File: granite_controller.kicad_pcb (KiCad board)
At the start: 4 copper layers, 230 x 40 mm, 204 parts, among them J1 HR911105A, J10 DRY_IN, J11 MB01_FP, J12 MB02_FP, J13 MB03_FP, J14 MB04_FP, J15 MB05_FP, J16 MB06_FP, J17 MB07_FP, J18 MB08_FP, J2 USB4105-xx-A, J3 19V_IN, J4 1WIRE, J5 1WIRE, J6 1WIRE, J7 1WIRE, J8 EXPANSION, J9 I2C_SENSOR, K1 TLP176AM, K10 TLP176AM, K11 TLP176AM, K12 TLP176AM, K13 TLP176AM, K14 TLP176AM, K15 TLP176AM, K16 TLP176AM, K2 TLP176AM, K3 TLP176AM, K4 TLP176AM, K5 TLP176AM, K6 TLP176AM, K7 TLP176AM, K8 TLP176AM, K9 TLP176AM, U1 ESP32-C6-WROOM-1-N8, U14 MCP23017-E/SO, U15 MCP23017-E/SO, U16 TLP290-4, U17 TLP290-4, U18 TPD4E05U06DQA, U2 TLV62569DBV, U3 W5500, U4 USBLC6-2SC6, U5 TMP1075D, U6 TPD4E05U06DQA, U7 TPD4E05U06DQA, U8 LMR51430YDDCR, Y2 25MHz 12pF YXC

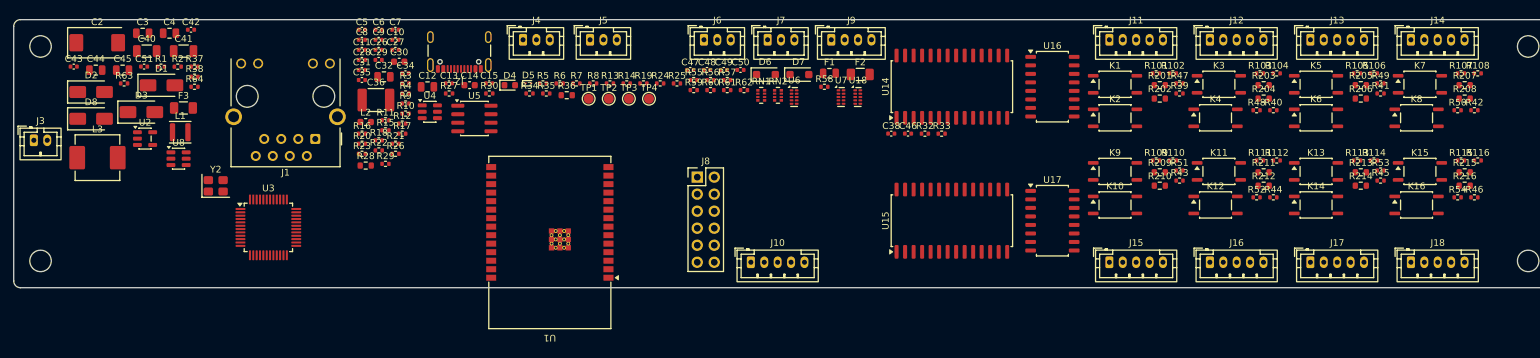
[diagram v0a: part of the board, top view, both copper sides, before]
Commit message: Tidy silkscreen after placement
tools/silk.py moves values to F.Fab, hides silk refs on small passives and
places the remaining refs clear of pads, silk outlines and courtyards,
connectors first. Silk DRC is clean apart from U1's intentional antenna
overhang. place.py keeps a label lane under J6/J7/J9.
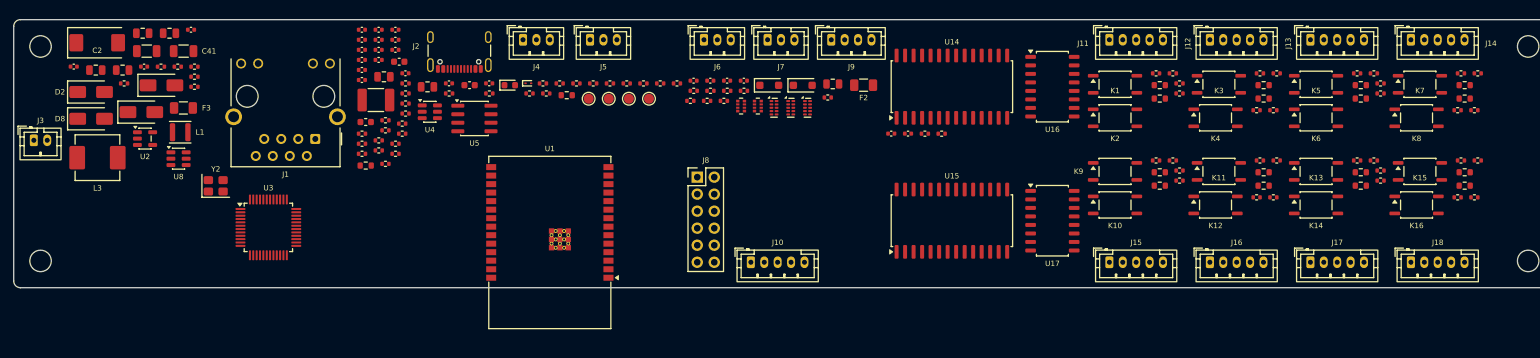
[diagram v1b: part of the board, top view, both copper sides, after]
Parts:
- moved R59 20.0 mm to (121.5, 11.6)
- moved R58 12.0 mm to (109.0, 10.6)
- moved U18 7.67 mm to (118.5, 13.1)
- moved U7 7.67 mm to (116.0, 13.1)
- moved R60 3.40 mm to (101.0, 12.1)
- moved R61 3.40 mm to (103.5, 12.1)
- moved R62 3.40 mm to (106.0, 12.1)
- moved RN1 3.40 mm to (108.5, 12.9)
- moved RN2 3.40 mm to (111.0, 12.9)
- moved U6 3.40 mm to (113.5, 13.1)
- moved C47 1.68 mm to (101.5, 9.11)
- moved C48 1.68 mm to (104.0, 9.11)
- moved C49 1.68 mm to (106.5, 9.11)
- moved C50 1.68 mm to (109.0, 9.11)
- moved D6 1.68 mm to (112.7, 9.79)
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
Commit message: 250 x 50 board, Ethernet placement, KRT routing, outer GND pours
- place.py: 250 x 50 mm with a 0.8 mm packing gap; Ethernet chain placed
  in line (W5500 rotated so its PHY pins face the RJ45, 33R row,
  termination/coupling row, crystal under XI/XO); label lanes under the
  top-edge connectors.
- setrules.py: signal vias 0.5/0.2, power/GND 0.6/0.3.
- krt_route.sh: KiCadRoutingTools chain on a copy outside the repo
  (planes, Ethernet and USB pairs, then the rest on F.Cu/B.Cu only).
- gndpour.py: GND pours on F.Cu/B.Cu plus 118 stitching vias.
- Board: user's hand placement, routed and poured. DRC: 0 parity, 21
  unconnected, 3 undersized vias at the W5500 crossovers, 11 dangling
  vias; see docs/handoff.md.
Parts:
- moved C27 71.1 mm to (74.4, 73.4), turned to 90 degrees
- moved C26 70.1 mm to (67.6, 73.4), turned to 90 degrees
- moved U5 69.7 mm to (129.5, 48.9)
- moved R27 65.3 mm to (123.0, 41.0)
- moved U6 63.6 mm to (170.0, 42.2)
- moved Y2 63.5 mm to (71.0, 73.4)
- moved RN2 63.1 mm to (167.0, 42.0)
- moved C11 62.9 mm to (58.0, 67.1)
- moved R30 62.7 mm to (126.0, 41.0)
- moved RN1 62.7 mm to (164.0, 42.0)
- moved R3 62.2 mm to (62.5, 71.6)
- moved R35 62.2 mm to (134.5, 40.1)
- moved C10 62.1 mm to (58.0, 65.1)
- moved J18 61.6 mm to (256.5, 74.8)
- moved C7 61.2 mm to (61.0, 62.6)
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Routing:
- net GND: track 0.00 -> 228.7 mm, vias 0 -> 191
- net +5V: track 0.00 -> 164.8 mm, vias 0 -> 9
- net I2C_INT_SDA: track 0.00 -> 153.2 mm, vias 0 -> 8
- net I2C_INT_SCL: track 0.00 -> 152.4 mm, vias 0 -> 12
- net EXP_INT: track 0.00 -> 136.1 mm, vias 0 -> 10
- net /Relay channels/NODE_ON8: track 0.00 -> 131.6 mm, vias 0 -> 4
- net VIN_SENSE: track 0.00 -> 129.4 mm, vias 0 -> 5
- net EXP_nRESET_INT: track 0.00 -> 123.7 mm, vias 0 -> 8
- net /Relay channels/RST_DRV4: track 0.00 -> 112.1 mm, vias 0 -> 8
- net /Relay channels/PWR_DRV4: track 0.00 -> 111.5 mm, vias 0 -> 10
- net /Relay channels/NODE_ON4: track 0.00 -> 111.2 mm, vias 0 -> 9
- net /Relay channels/PWR_DRV8: track 0.00 -> 104.7 mm, vias 0 -> 8
- net +3V3: track 0.00 -> 103.5 mm, vias 0 -> 36
- net /Relay channels/NODE_ON2: track 0.00 -> 102.9 mm, vias 0 -> 12
- net /Relay channels/NODE_ON3: track 0.00 -> 99.3 mm, vias 0 -> 10
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- added copper zone on In2.Cu, net +3V3
- added copper zone on B.Cu, net GND
- added copper zone on F.Cu, net GND
- added copper zone on In1.Cu, net GND
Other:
- board size 230 x 40 mm -> 250 x 50 mm

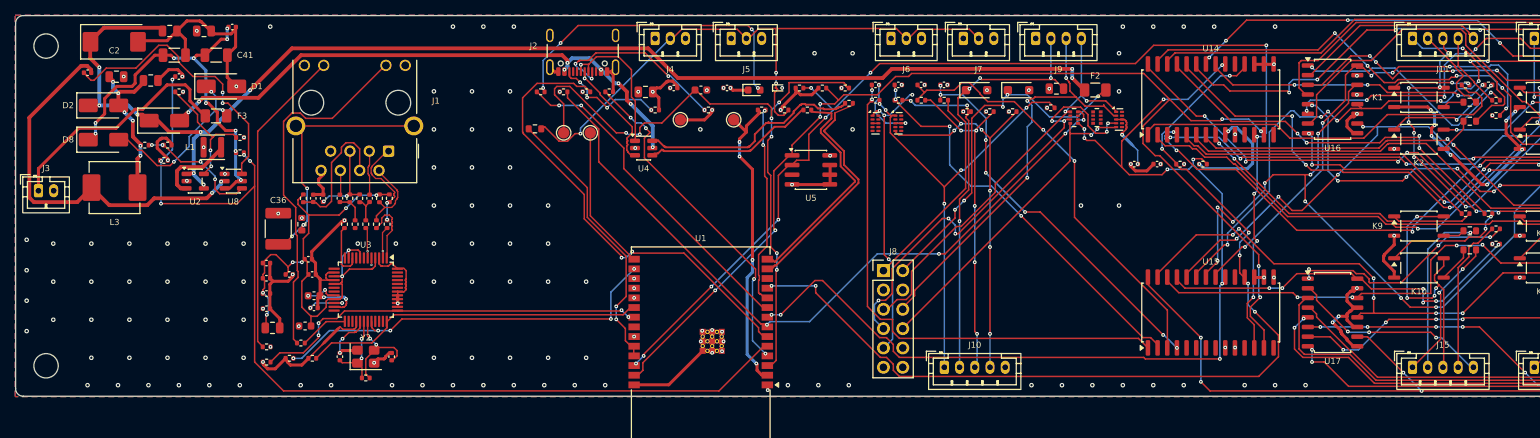
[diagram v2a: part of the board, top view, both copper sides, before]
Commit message: Targeted KRT reroute of the open nets; handoff update
Ripped and re-routed the 16 open signal nets with everything else kept,
then a GND pass without rip-up. Closed ETH_RXN, USB_CONN_D+ and HDR_IO5:
21 -> 18 unconnected, violations unchanged (27). The rest is blocked by
neighbouring copper and the RN1/RN2/U7/U18 pad field around J8.

docs/handoff.md: current board state, next steps (spread J8 area, re-run
the targeted pass, hand-route critical nets) and the pod/duck
architecture under discussion.
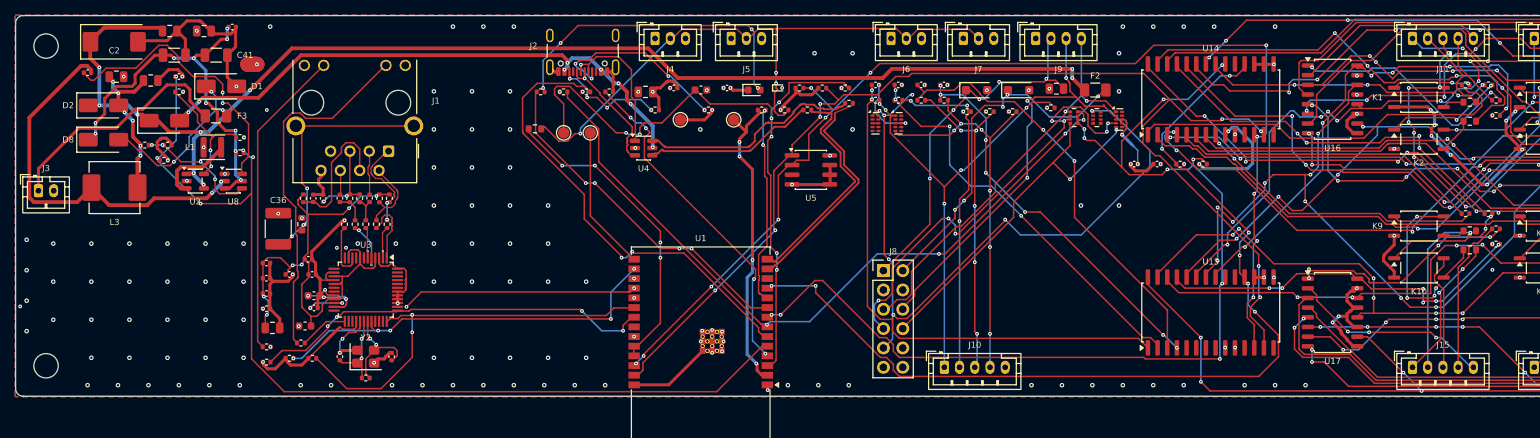
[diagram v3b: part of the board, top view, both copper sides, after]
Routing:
- net /Expansion header/HDR_IO5: track 38.4 -> 94.1 mm, vias 4 -> 7
- net ETH_MOSI: track 0.00 -> 30.9 mm, vias 1 -> 2
- net GND: track 228.7 -> 244.8 mm, vias 191 -> 197
- net ETH_INT: track 44.4 -> 54.7 mm, vias 0 -> 2
- net /Expansion header/HDR_INT: track 42.7 -> 48.7 mm
- net /Ethernet/ETH_RXN: track 0.05 -> 5.71 mm, vias 1 -> 2
- net /MCU/OW_MCU: track 36.4 -> 40.3 mm, vias 2 -> 4
- net /Ethernet/+3V3A: track 70.5 -> 67.8 mm, vias 8 -> 6
- net VIN_SENSE: track 129.4 -> 127.3 mm
- net /MCU/LED_HB: track 43.1 -> 45.1 mm, vias 2 -> 4
- net /MCU/USB_CONN_D+: track 15.9 -> 17.5 mm
- net ETH_RST: track 51.2 -> 52.4 mm
- net /Expansion header/HDR_3V3: track 47.8 -> 47.7 mm, vias 3 -> 5

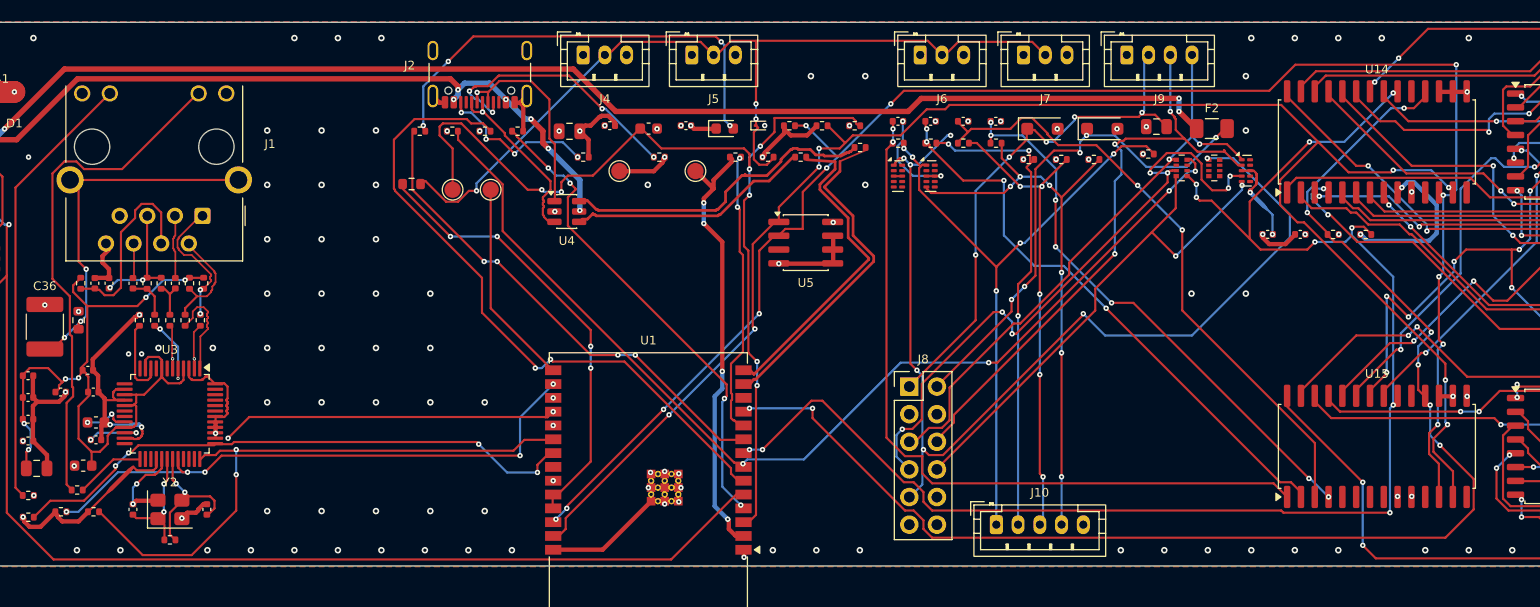
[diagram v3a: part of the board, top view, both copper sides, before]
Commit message: Spread the J8 part field and rerun the targeted KRT pass
Moved RN1/RN2 between U1 and J8 (rot 180, MCU side facing U1), U7 next to
J8 pins 9-11 and U18 above J10. Strapped the TPD4E05 centre GND pads to a
plane via, cleared all copper of the 22 affected nets (KRT's own rip left
stubs) and rerouted them, then a GND pass. DRC: 18 -> 7 unconnected,
27 -> 23 violations, 0 parity, no shorts or dangling tracks.

tools/krt_reroute.sh captures the targeted pass for next time.
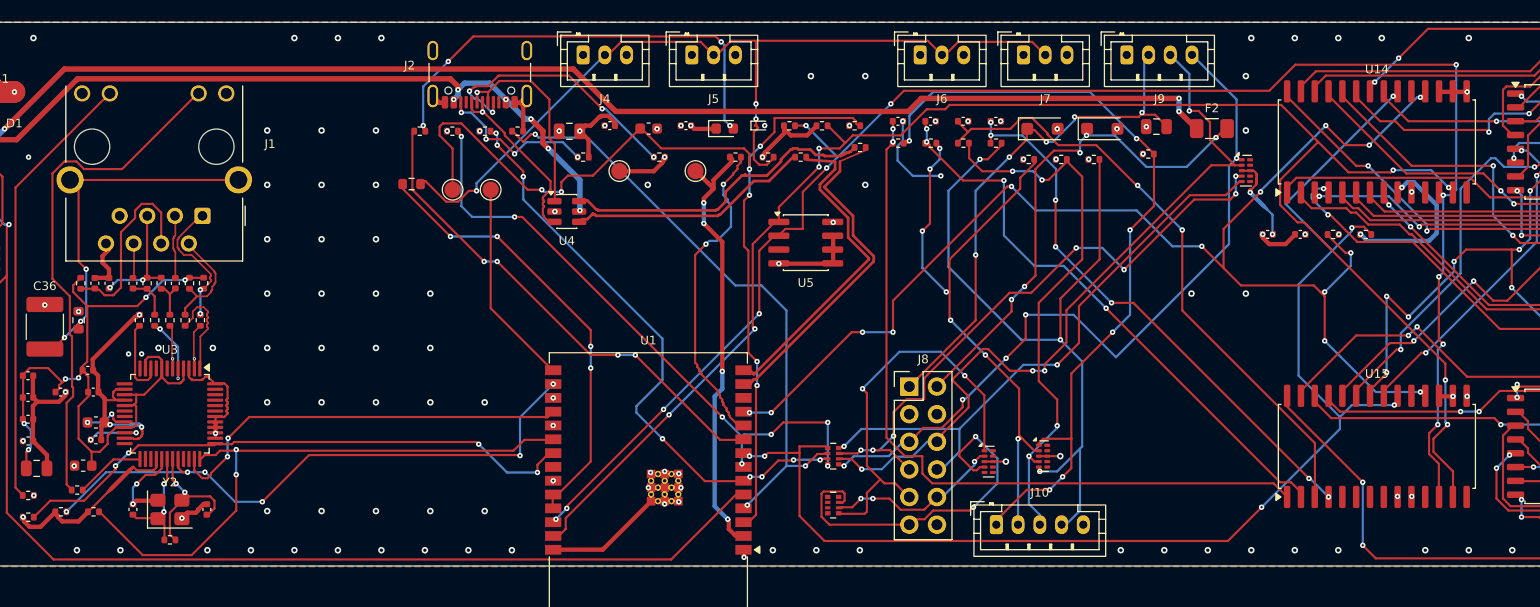
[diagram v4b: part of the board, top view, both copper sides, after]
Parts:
- moved RN2 46.8 mm to (132.0, 73.0), turned to 180 degrees
- moved RN1 41.6 mm to (132.0, 68.5), turned to 180 degrees
- moved U18 27.8 mm to (151.3, 68.5)
- moved U7 27.5 mm to (146.3, 69.0)
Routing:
- net /Expansion header/HDR_IO5: track 94.1 -> 37.9 mm, vias 7 -> 2
- net I2C_EXT_SCL: track 96.1 -> 56.3 mm, vias 4 -> 7
- net /Expansion header/HDR_IO15: track 0.00 -> 33.4 mm, vias 0 -> 2
- net EXP_INT: track 136.1 -> 118.6 mm, vias 10 -> 6
- net /Expansion header/HDR_IO8: track 0.00 -> 15.8 mm, vias 0 -> 3
- net /Expansion header/DRYC4: track 52.8 -> 68.0 mm, vias 6 -> 3
- net /Expansion header/DRYC1: track 58.3 -> 72.8 mm, vias 5 -> 6
- net /Expansion header/HDR_SCL: track 53.4 -> 67.6 mm, vias 2 -> 5
- net /Expansion header/HDR_SDA: track 56.0 -> 69.3 mm, vias 3 -> 4
- net /Expansion header/DRYC2: track 44.6 -> 56.7 mm, vias 3 -> 7
- net EXP_nRESET: track 44.9 -> 56.1 mm, vias 4 -> 3
- net I2C_EXT_SDA: track 61.1 -> 53.1 mm, vias 2 -> 8
- net /Expansion header/DRYC3: track 43.5 -> 50.7 mm, vias 5 -> 4
- net ETH_MOSI: track 30.9 -> 37.9 mm
- net /Expansion header/HDR_INT: track 48.7 -> 53.2 mm
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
